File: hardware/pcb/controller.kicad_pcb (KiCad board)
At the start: 2 copper layers, 8 parts, among them U1 ESP32-WROOM-32, U2 SX1262IMLTRT, U4 PE4259, U5 AP2112K-3.3, U6 NHD-C12832A1Z-FSRGB

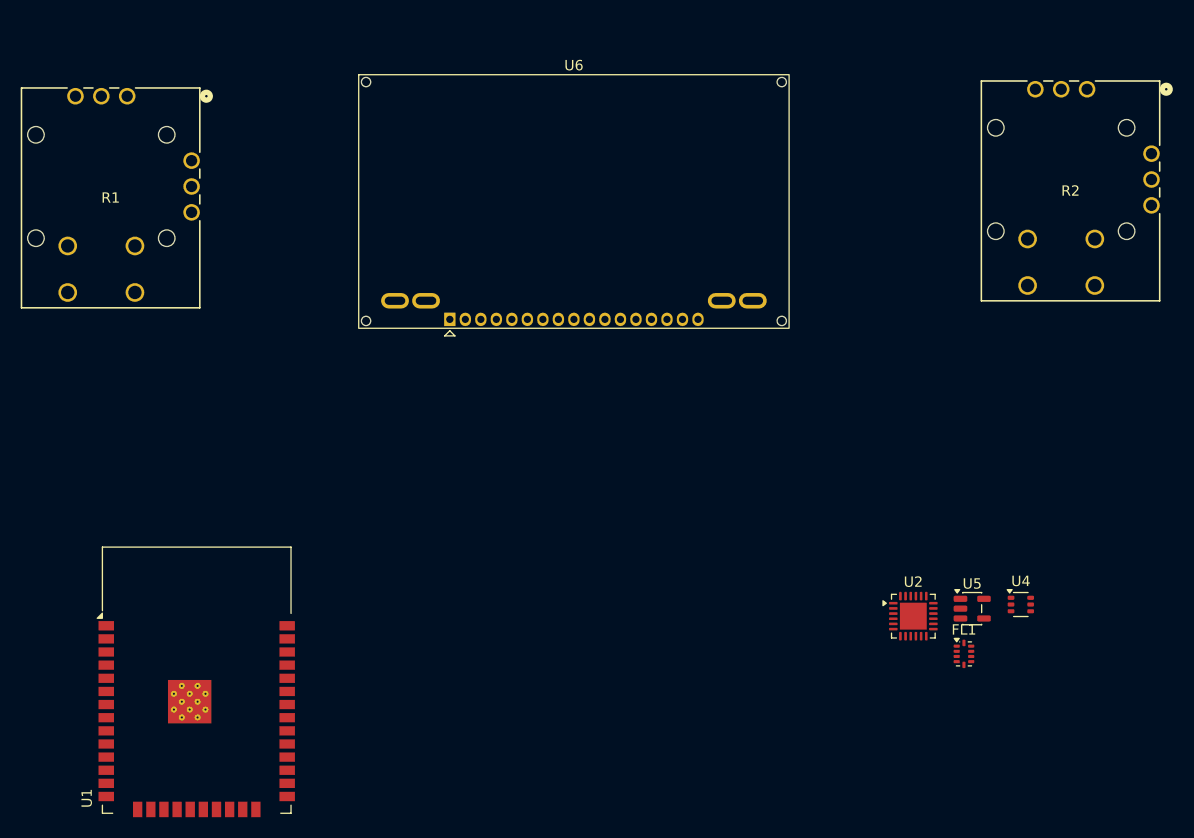
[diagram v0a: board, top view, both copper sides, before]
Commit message: started wiring schematic
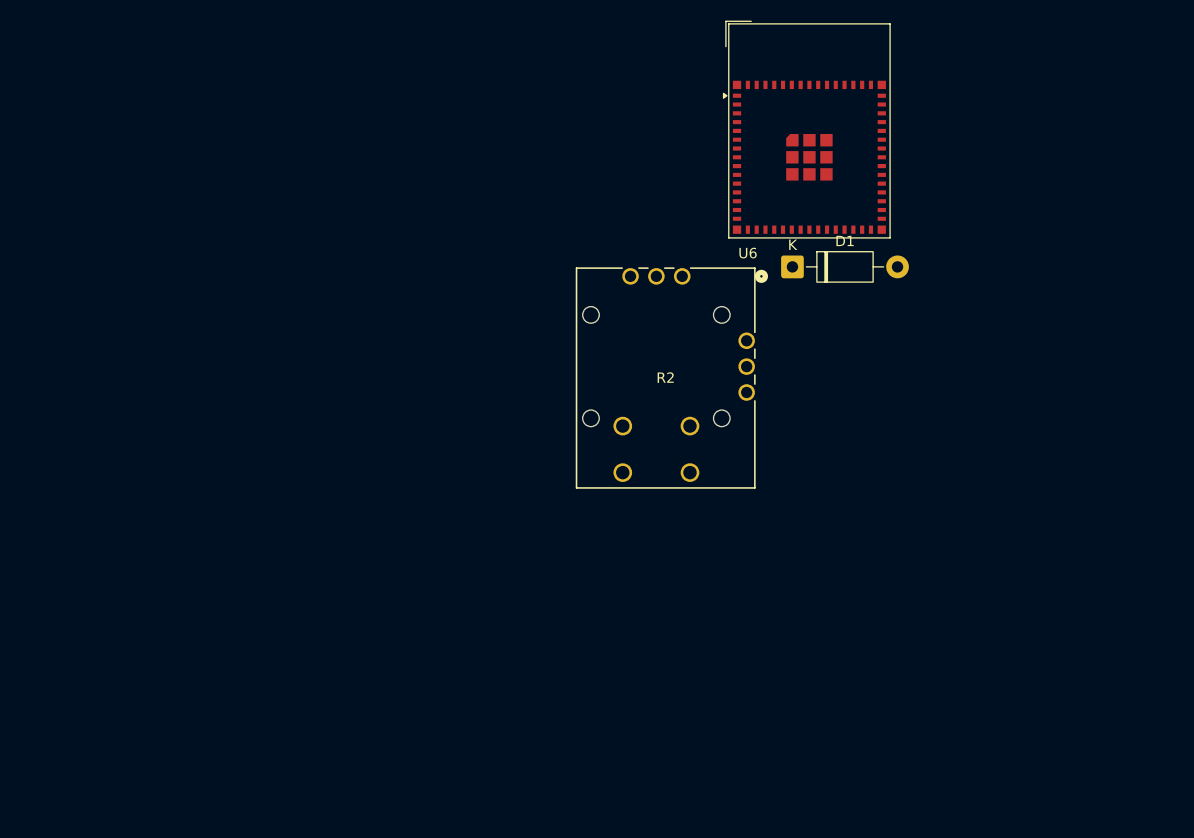
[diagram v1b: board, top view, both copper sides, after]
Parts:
- removed FL1: 0900FM15K0039, RF_Converter:Balun_Johanson_0900FM15K0039
- removed R1: THB001P, Imports:THB001P_CNK
- removed U1: ESP32-WROOM-32, RF_Module:ESP32-WROOM-32
- removed U2: SX1262IMLTRT, Package_DFN_QFN:QFN-24-1EP_4x4mm_P0.5mm_EP2.6x2.6mm
- removed U4: PE4259, Package_TO_SOT_SMD:SOT-363_SC-70-6
- removed U5: AP2112K-3.3, Package_TO_SOT_SMD:SOT-23-5
- added D1: 1N5819, Diode_THT:D_DO-41_SOD81_P10.16mm_Horizontal, F.Cu at (163.1, 107.7)
- U6: value NHD-C12832A1Z-FSRGB -> ESP32-S3-MINI-1; footprint Display:NHD-C12832A1Z-FSRGB -> RF_Module:ESP32-S2-MINI-1
- moved R2 43.1 mm to (152.5, 108.6)
- moved U6 39.3 mm to (164.8, 94.5)
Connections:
- R2 pad 1: unconnected-(R2-Pad1) -> +3.3V
- R2 pad 1': unconnected-(R2-Pad1') -> +3.3V
- R2 pad 2: unconnected-(R2-Pad2) -> /JOY_2_X
- R2 pad 2': unconnected-(R2-Pad2') -> /JOY_2_Y
- R2 pad 3: unconnected-(R2-Pad3) -> GND
- R2 pad 3': unconnected-(R2-Pad3') -> GND
- R2 pad B: unconnected-(R2-PadB) -> GND
- R2 pad C: unconnected-(R2-PadC) -> /JOY_2_BTN
- U6 pad 1: unconnected-(U6-V0-Pad1) -> GND
- U6 pad 2: unconnected-(U6-V1-Pad2) -> GND
- U6 pad 3: unconnected-(U6-V2-Pad3) -> +3.3V
- U6 pad 4: unconnected-(U6-V3-Pad4) -> /JOY_1_BTN
- U6 pad 5: unconnected-(U6-V4-Pad5) -> /JOY_2_BTN
- U6 pad 6: unconnected-(U6-C2--Pad6) -> /JOY_1_X
- U6 pad 7: unconnected-(U6-C2+-Pad7) -> /JOY_1_Y
- U6 pad 8: unconnected-(U6-C1+-Pad8) -> /JOY_2_X
- U6 pad 9: unconnected-(U6-C1--Pad9) -> /JOY_2_Y
